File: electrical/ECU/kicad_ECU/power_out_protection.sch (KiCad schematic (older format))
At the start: 15 parts

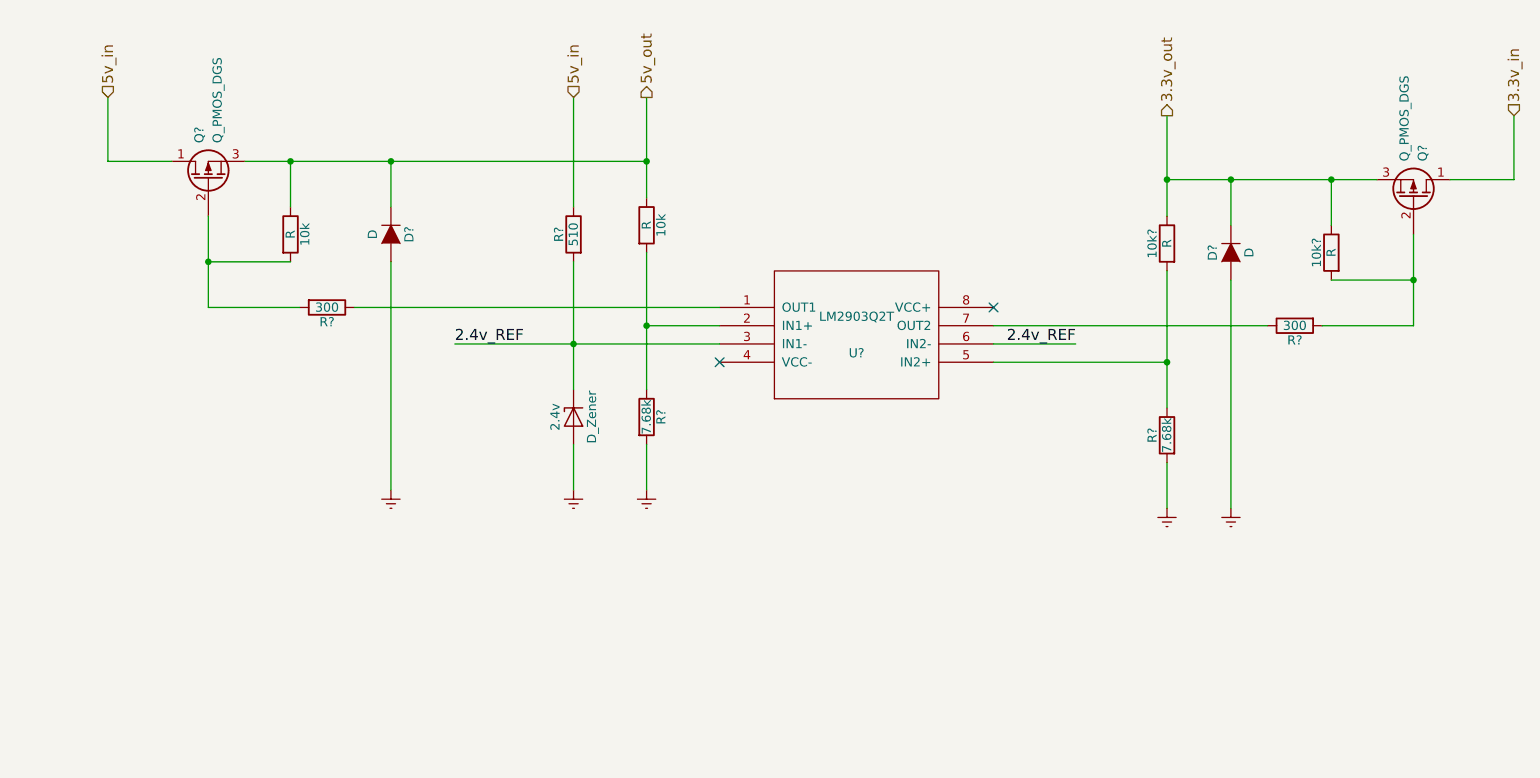
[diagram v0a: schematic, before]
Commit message: fixed some naming errors and initial round of double checking
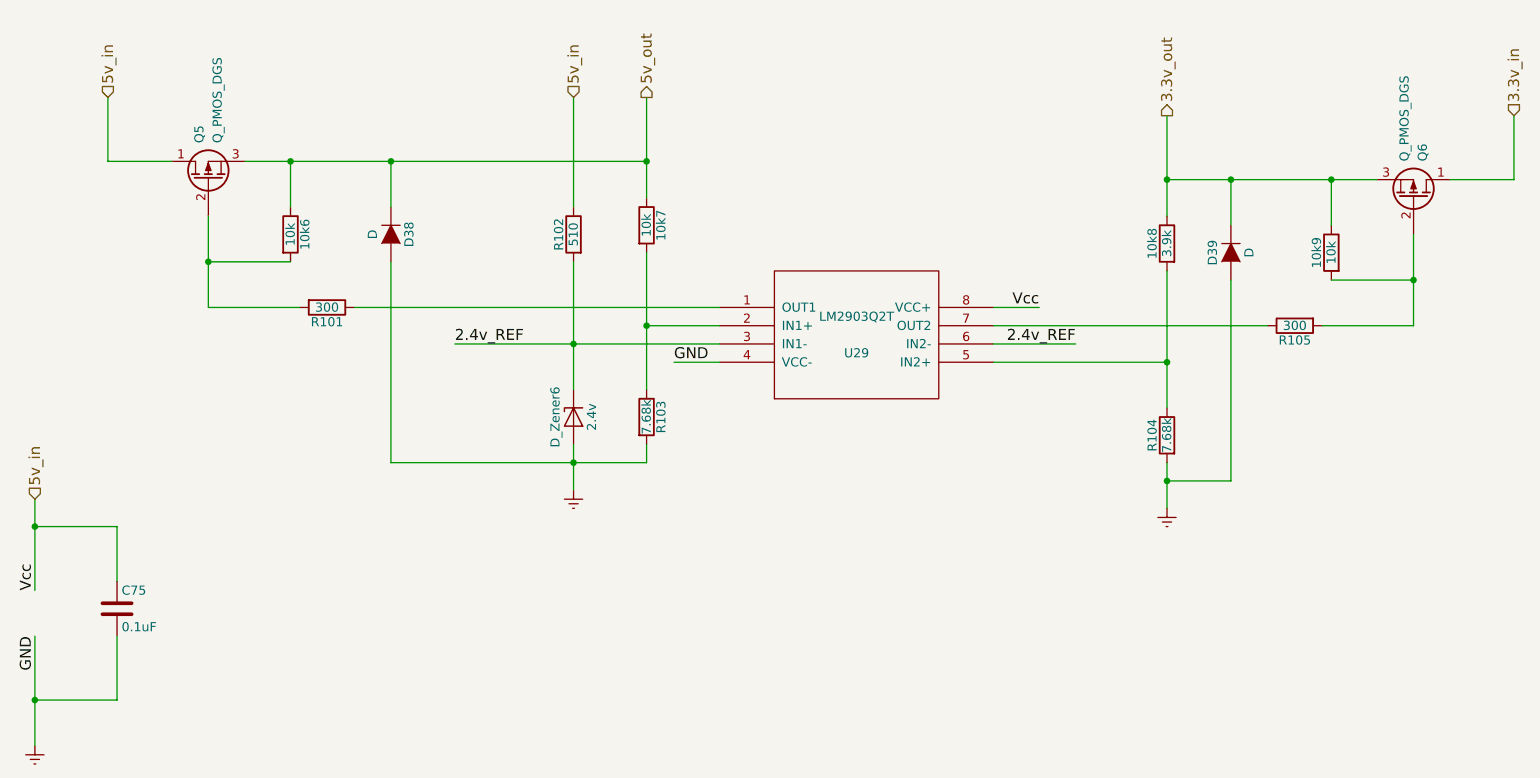
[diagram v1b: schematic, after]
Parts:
- added C26: 0.1uF, symbol C
- 10k2, 10k3: renamed from 10k; value R -> 10k
- 10k4: renamed from 10k?; value R -> 3.9k
- 10k5: renamed from 10k?; value R -> 10k
- D_Zener1: renamed from 2.4v; value D_Zener -> 2.4v
- gave numbers to parts that had none: 10
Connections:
- net 5v_in: now also U9.8 (VCC+), C26.1
- net Earth: now also U9.4 (VCC-), C26.2
- no-connect marks 2 -> 0
